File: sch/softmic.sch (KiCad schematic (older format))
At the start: 79 parts, among them J1 USB-C, J2 Conn_01x03, J3 XLR-OUT, J4 AudioJack3_Ground, P1 4V1, P2 4V1, P3 VccPad, P4 4V1, P5 4V1, P6 4V1, Q1 MMBFJ201, Q2 BSS64AT116, SW1 SW_Push, SW2 SW_Push, U1 MCP1812BT-033, U2 MCP2221A, U3 OPA1671, U4 OPA1671, U5 BQ21040, U6 MAX11613, U7 Oled_128_32, U8 ESP32-WROOM

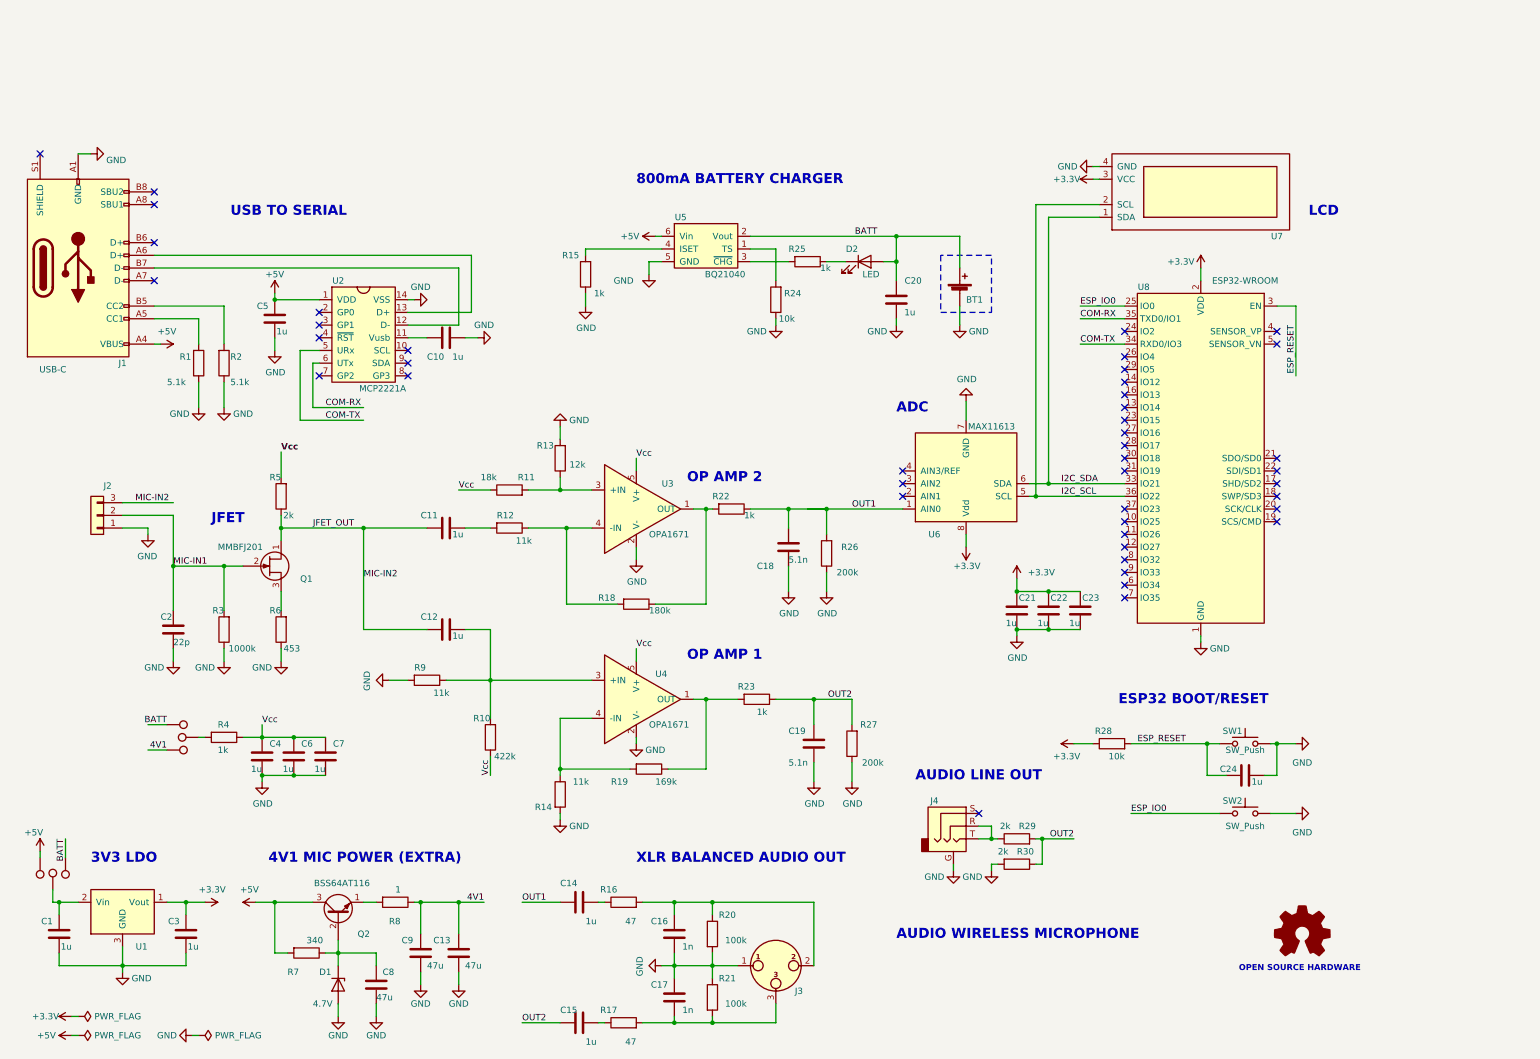
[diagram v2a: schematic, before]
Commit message: changed USB to serial IC, changed some footprints, changed RST SW
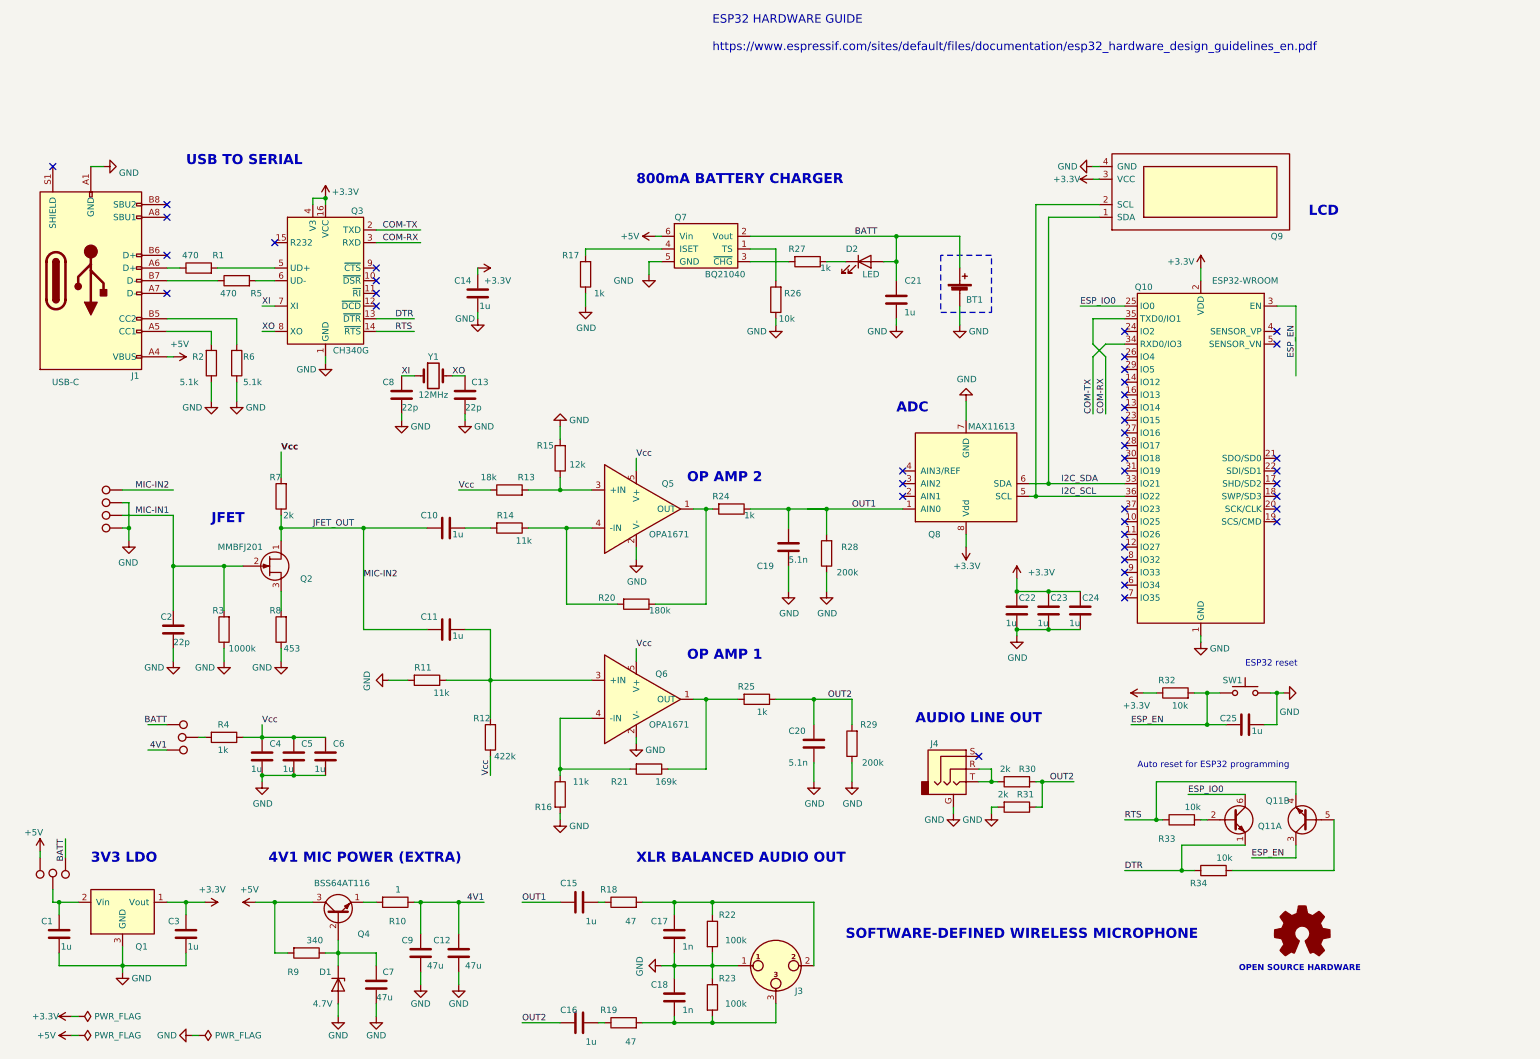
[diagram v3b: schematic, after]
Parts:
- removed C10: 1u, Capacitor_SMD:C_0603_1608Metric, symbol Device:C
- removed J2: Conn_01x03, Connector_PinHeader_2.54mm:PinHeader_1x03_P2.54mm_Vertical, symbol Connector_Generic:Conn_01x03
- removed SW2: SW_Push, Button_Switch_SMD:SW_SPST_TL3305A, symbol Switch:SW_Push
- removed U2: MCP2221A, Package_SO:TSSOP-14_4.4x5mm_P0.65mm, symbol MCP2221A:MCP2221A
- added C13, C8: 22p, Capacitor_SMD:C_0603_1608Metric, symbol Device:C
- added P? (x4): none, TestPoint:TestPoint_THTPad_D1.5mm_Drill0.7mm, symbol Connector:TestPoint
- added Q11: BC847BS-TP, Package_TO_SOT_SMD:SOT-363_SC-70-6, symbol Transistor_BJT:BC847BS
- added Q3: CH340G, Package_SO:SOIC-16_3.9x9.9mm_P1.27mm, symbol Interface_USB:CH340G
- added R1, R5: 470, Resistor_SMD:R_0603_1608Metric, symbol Device:R
- added R33, R34: 10k, Resistor_SMD:R_0603_1608Metric, symbol Device:R
- added Y1: 12MHz, Crystal:Crystal_SMD_5032-2Pin_5.0x3.2mm, symbol Device:Crystal
- BT1: Description (none) -> Litium Battery 1 Cell, 4.2V
- C2: Mouser PN 80-C0603C220J1G -> none; Mouser Price $0.10 -> none
- J4: value AudioJack3_Ground -> AudioJack 3.5mm; Description (none) -> 3.5mm Audio Jack; Digikey PN (none) -> CP-43514SJCT-ND; Digikey Price (none) -> 1.16$; LCSC PN (none) -> none; LCSC Price (none) -> none; MPN (none) -> SJ-43514-SMT-TR; Manufacturer (none) -> Cui Devices; Mouser PN (none) -> 490-SJ-43514-SMT-TR; Mouser Price (none) -> 0.95€
- P1: renamed from P4; footprint TestPoint:TestPoint_Pad_D1.0mm -> TestPoint:TestPoint_THTPad_D1.5mm_Drill0.7mm
- P2: renamed from P5; footprint TestPoint:TestPoint_Pad_D1.0mm -> TestPoint:TestPoint_THTPad_D1.5mm_Drill0.7mm
- P3: renamed from P6; footprint TestPoint:TestPoint_Pad_D1.0mm -> TestPoint:TestPoint_THTPad_D1.5mm_Drill0.7mm
- P4: renamed from P1; footprint TestPoint:TestPoint_Pad_D1.0mm -> TestPoint:TestPoint_THTPad_D1.5mm_Drill0.7mm
- P5: renamed from P2; footprint TestPoint:TestPoint_Pad_D1.0mm -> TestPoint:TestPoint_THTPad_D1.5mm_Drill0.7mm
- P6: renamed from P3; footprint TestPoint:TestPoint_Pad_D1.0mm -> TestPoint:TestPoint_THTPad_D1.5mm_Drill0.7mm
- SW1: value SW_Push -> RST; footprint Button_Switch_SMD:SW_SPST_TL3305A -> Button_Switch_SMD:SW_SPST_FSMSM; Description Switch Tactile SPST-NO 0.05A 24V -> Tactile Switches Tact 50mA 12VDC, 6.0x3.5, 4.3mm H, Black A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; Digikey PN 679-2212-ND -> none; Digikey Price $2.99 -> none; MPN 3CSH9 -> PTS636SM43SMTRLF; Manufacturer Apem -> C&K; Mouser PN 642-3CSH9 -> 611-PTS636SM43SMTRLF; Mouser Price $2.70 -> $0.10
- renumbered C11 to C10, C12 to C11, C13 to C12, C5 to C14, C14 to C15, C15 to C16, C16 to C17, C17 to C18, C18 to C19, C19 to C20, C20 to C21, C21 to C22, C22 to C23, C23 to C24, C24 to C25, C6 to C5, C7 to C6, C8 to C7, U1 to Q1, U8 to Q10, Q1 to Q2, Q2 to Q4, U3 to Q5, U4 to Q6, U5 to Q7, U6 to Q8, U7 to Q9, R8 to R10, R9 to R11, R10 to R12, R11 to R13, R12 to R14, R13 to R15, R14 to R16, R15 to R17, R16 to R18, R17 to R19, R1 to R2, R18 to R20, R19 to R21, R20 to R22, R21 to R23, R22 to R24, R23 to R25, R24 to R26, R25 to R27, R26 to R28, R27 to R29, R29 to R30, R30 to R31, R28 to R32, R2 to R6, R5 to R7, R6 to R8, R7 to R9
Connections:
- net labels added: DTR, ESP_EN, RTS, XI, XO
- net labels removed: ESP_RESET
- wire segments 230 -> 253
- no-connect marks 43 -> 41
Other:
- note added: "Auto reset for ESP32 programming"
- note added: "ESP32 HARDWARE GUIDE\n\nhttps://www.espressif.com/sites/default/files/documentation/esp32_hardware_design_guidelines_en.pdf"
- note added: "ESP32 reset"
- note added: "SOFTWARE-DEFINED WIRELESS MICROPHONE"
- note removed: "AUDIO WIRELESS MICROPHONE"
- note removed: "ESP32 BOOT/RESET\n"
- moved on the sheet: C14, C25, J1, J4, R2, R30, R31, R32, R6, SW1

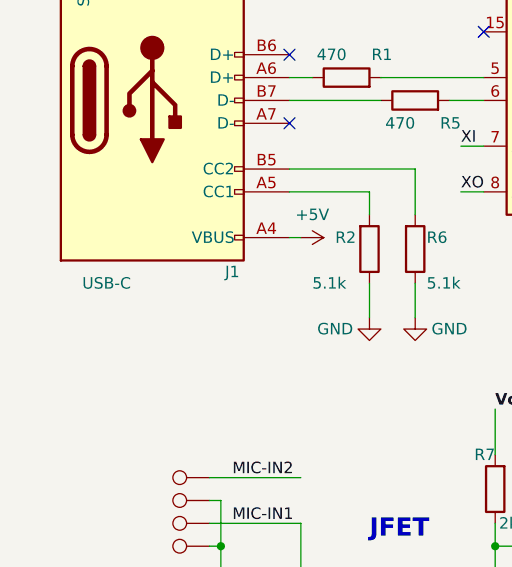
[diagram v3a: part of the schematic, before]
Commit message: changed USB-C connector type
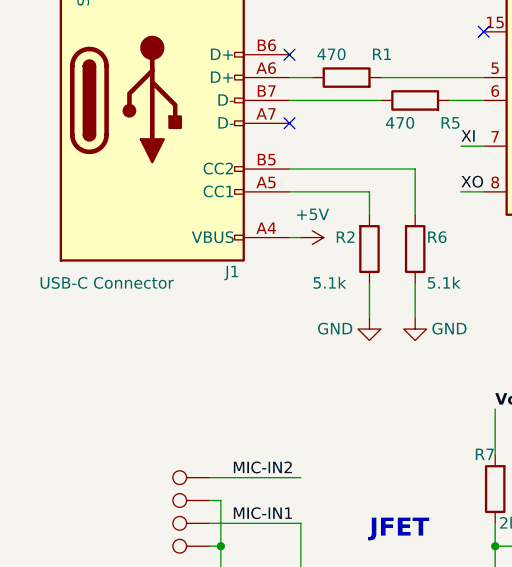
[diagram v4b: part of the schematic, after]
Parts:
- J1: value USB-C -> USB-C Connector; footprint footprint:USB-10137061-00021LF -> Connector_USB:USB_C_Receptacle_GCT_USB4085; Digikey PN 609-6444-1-ND -> 2073-USB4085-GF-ACT-ND; Digikey Price $2.26 -> $1.1; MPN 10137061-00021LF -> USB4085-GF-A; Manufacturer Amphenol -> GCT; Mouser PN 649-10137061-00021LF -> none; Mouser Price $2.20 -> none
- gave numbers to parts that had none: 4
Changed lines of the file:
@@
 P 1150 1650
 F 0 "J1" H 1500 2400 50  0000 C CNN
-F 1 "USB-C" H 950 2450 50  0000 C CNN
-F 2 "footprint:USB-10137061-00021LF" H 1300 1650 50  0001 C CNN
-F 3 "https://www.usb.org/sites/default/files/documents/usb_type-c.zip" H 1300 1650 50  0001 C CNN
-F 4 "Amphenol" H 1150 1650 50  0001 C CNN "Manufacturer"
-F 5 "10137061-00021LF" H 1150 1650 50  0001 C CNN "MPN"
+F 1 "USB-C Connector" H 950 2450 50  0000 C CNN
+F 2 "Connector_USB:USB_C_Receptacle_GCT_USB4085" H 1300 1650 50  0001 C CNN
+F 3 "https://gct.co/files/drawings/usb4085.pdf" H 1300 1650 50  0001 C CNN
+F 4 "GCT" H 1150 1650 50  0001 C CNN "Manufacturer"
+F 5 "USB4085-GF-A" H 1150 1650 50  0001 C CNN "MPN"
 F 6 "USB Connectors USB 3.1 Receptacle" H 1150 1650 50  0001 C CNN "Description"
-F 7 "609-6444-1-ND" H 1150 1650 50  0001 C CNN "Digikey PN"
-F 8 "$2.26" H 1150 1650 50  0001 C CNN "Digikey Price"
-F 9 "649-10137061-00021LF" H 1150 1650 50  0001 C CNN "Mouser PN"
-F 10 "$2.20" H 1150 1650 50  0001 C CNN "Mouser Price"
+F 7 "2073-USB4085-GF-ACT-ND " H 1150 1650 50  0001 C CNN "Digikey PN"
+F 8 "$1.1" H 1150 1650 50  0001 C CNN "Digikey Price"
+F 9 "none" H 1150 1650 50  0001 C CNN "Mouser PN"
+F 10 "none" H 1150 1650 50  0001 C CNN "Mouser Price"
 F 11 "none" H 1150 1650 50  0001 C CNN "LCSC PN"
 F 12 "none" H 1150 1650 50  0001 C CNN "LCSC Price"
@@
 ESP32 reset
 $Comp
-L Connector:TestPoint P?
+L Connector:TestPoint P10
 U 1 1 5EA549ED
 P 1400 3600
-F 0 "P?" H 1400 3650 50  0001 L CNN
+F 0 "P10" H 1400 3650 50  0001 L CNN
 F 1 "none" V 1500 3600 50  0001 L CNN
 F 2 "TestPoint:TestPoint_THTPad_D1.5mm_Drill0.7mm" H 1600 3600 50  0001 C CNN
@@
 $EndComp
 $Comp
-L Connector:TestPoint P?
+L Connector:TestPoint P7
 U 1 1 5EA53BD8
 P 1400 3300
-F 0 "P?" H 1400 3350 50  0001 L CNN
+F 0 "P7" H 1400 3350 50  0001 L CNN
 F 1 "none" V 1500 3300 50  0001 L CNN
 F 2 "TestPoint:TestPoint_THTPad_D1.5mm_Drill0.7mm" H 1600 3300 50  0001 C CNN
@@
 	1800 3500 1800 3900
 $Comp
-L Connector:TestPoint P?
+L Connector:TestPoint P9
 U 1 1 5EA5476A
 P 1400 3500
-F 0 "P?" H 1400 3550 50  0001 L CNN
+F 0 "P9" H 1400 3550 50  0001 L CNN
 F 1 "none" V 1500 3500 50  0001 L CNN
 F 2 "TestPoint:TestPoint_THTPad_D1.5mm_Drill0.7mm" H 1600 3500 50  0001 C CNN
@@
 $EndComp
 $Comp
-L Connector:TestPoint P?
+L Connector:TestPoint P8
 U 1 1 5EA550E3
 P 1400 3400
-F 0 "P?" H 1400 3450 50  0001 L CNN
+F 0 "P8" H 1400 3450 50  0001 L CNN
 F 1 "none" V 1500 3400 50  0001 L CNN
 F 2 "TestPoint:TestPoint_THTPad_D1.5mm_Drill0.7mm" H 1600 3400 50  0001 C CNN

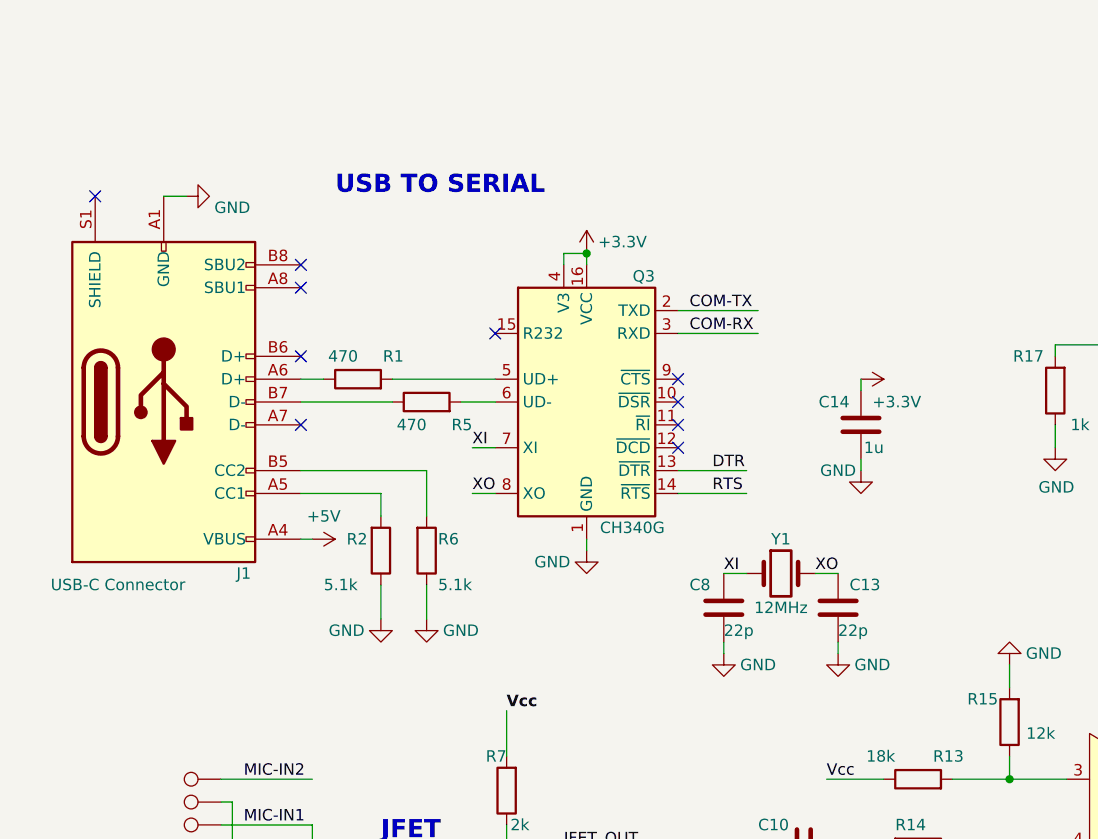
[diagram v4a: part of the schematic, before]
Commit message: changed USB-C footprint and battery holder
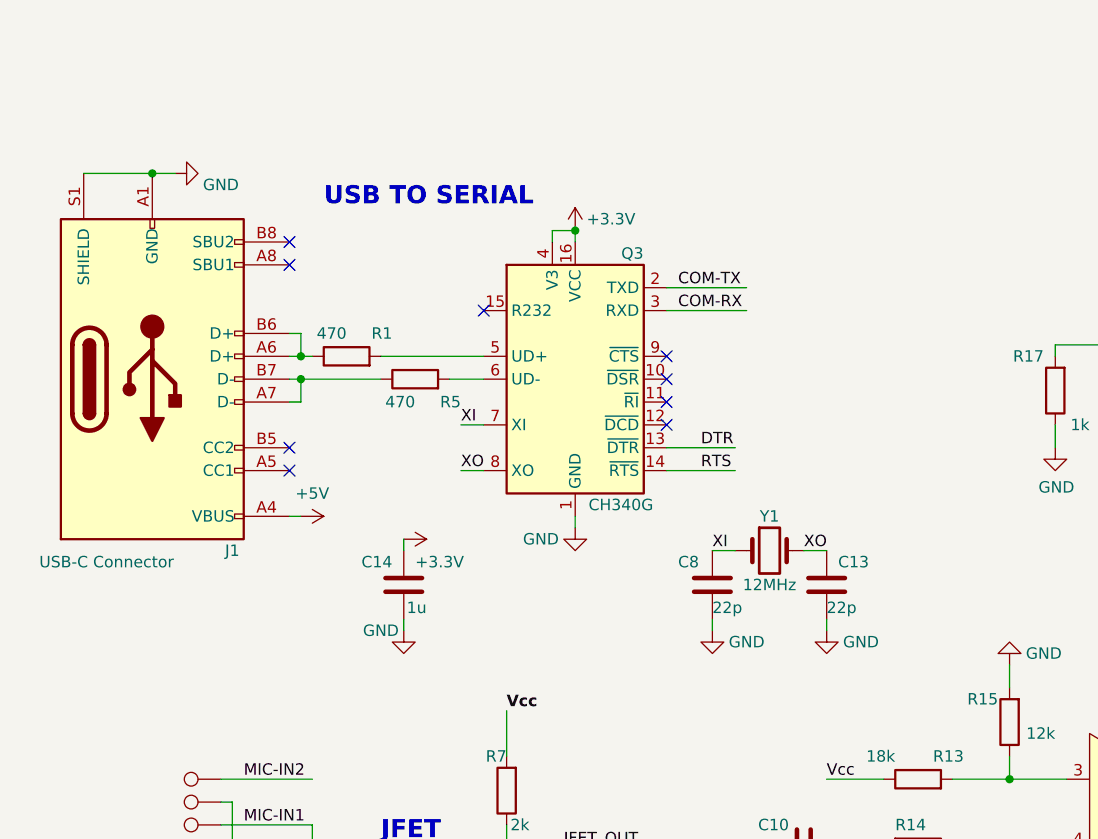
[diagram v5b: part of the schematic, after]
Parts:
- removed R2, R6: 5.1k, Resistor_SMD:R_0603_1608Metric, symbol Device:R
- added logo1: Logo_Open_Hardware_Small, Symbol:OSHW-Logo2_7.3x6mm_SilkScreen, symbol Graphic:Logo_Open_Hardware_Small
- BT1: footprint Battery:BatteryHolder_Keystone_1042_1x18650 -> footprint:BatteryHolder18650
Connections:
- wire segments 253 -> 254
- no-connect marks 41 -> 40
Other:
- moved on the sheet: C13, C14, C8, J1, Q3, R1, R5, Y1
